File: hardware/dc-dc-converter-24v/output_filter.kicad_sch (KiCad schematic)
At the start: 3 parts

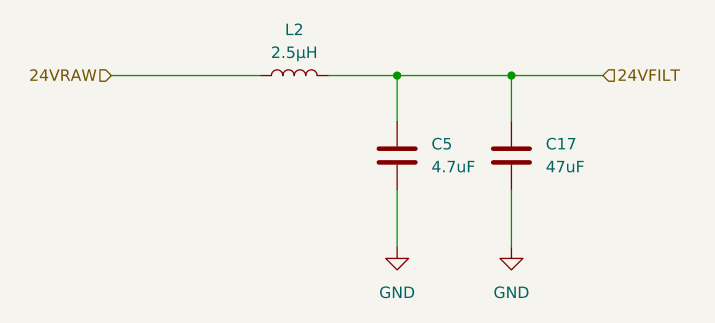
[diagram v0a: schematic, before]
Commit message: create layout for DC-DC converter
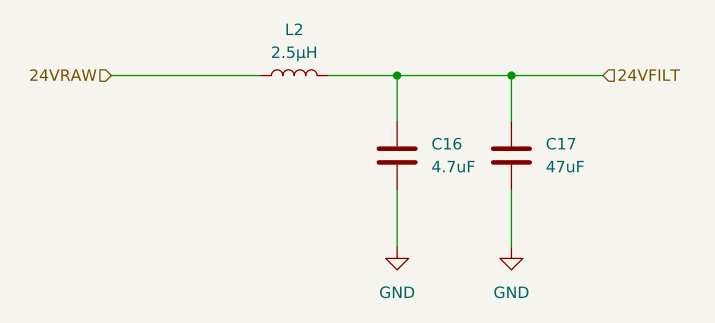
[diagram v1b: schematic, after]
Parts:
- renumbered C5 to C16
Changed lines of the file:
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@@
   (symbol (lib_id "power:GND") (at 118.11 66.04 0) (unit 1)
     (in_bom yes) (on_board yes) (dnp no) (fields_autoplaced)
-    (property "Reference" "#PWR05" (at 118.11 72.39 0)
+    (property "Reference" "#PWR031" (at 118.11 72.39 0)
       (effects (font (size 1.27 1.27)) hide)
     )
@@
       (project "dc-dc-converter-24v"
         (path "/f3858519-f688-4645-91dc-9843c9d0ed53/8f8f2bb4-fdfe-4421-bc8c-e8dc6b7f806e"
-          (reference "#PWR05") (unit 1)
+          (reference "#PWR031") (unit 1)
         )
       )
@@
   (symbol (lib_id "benediktibk:C_4_7uF_SMD_0805_50V_10%") (at 118.11 55.88 0) (unit 1)
     (in_bom yes) (on_board yes) (dnp no) (fields_autoplaced)
-    (property "Reference" "C5" (at 121.92 54.61 0)
+    (property "Reference" "C16" (at 121.92 54.61 0)
       (effects (font (size 1.27 1.27)) (justify left))
     )
@@
       (project "dc-dc-converter-24v"
         (path "/f3858519-f688-4645-91dc-9843c9d0ed53/8f8f2bb4-fdfe-4421-bc8c-e8dc6b7f806e"
-          (reference "C5") (unit 1)
+          (reference "C16") (unit 1)
         )
       )
@@
   (symbol (lib_id "power:GND") (at 130.81 66.04 0) (unit 1)
     (in_bom yes) (on_board yes) (dnp no) (fields_autoplaced)
-    (property "Reference" "#PWR024" (at 130.81 72.39 0)
+    (property "Reference" "#PWR032" (at 130.81 72.39 0)
       (effects (font (size 1.27 1.27)) hide)
     )
@@
       (project "dc-dc-converter-24v"
         (path "/f3858519-f688-4645-91dc-9843c9d0ed53/8f8f2bb4-fdfe-4421-bc8c-e8dc6b7f806e"
-          (reference "#PWR024") (unit 1)
+          (reference "#PWR032") (unit 1)
         )
       )

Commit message: fix RS order number
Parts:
- L2: RS order number 238-3683 -> 238-3683
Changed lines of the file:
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@@
       (effects (font (size 1.27 1.27)) hide)
     )
-    (property "RS order number" " 238-3683" (at 106.68 46.99 0)
+    (property "RS order number" "238-3683" (at 106.68 46.99 0)
       (effects (font (size 1.27 1.27)) hide)
     )
